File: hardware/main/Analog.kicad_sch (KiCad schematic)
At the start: 51 parts, among them J302 Overvoltage_protection, J303 Rad_sensor, J304 Mos_temp, J305 Mos_temp, U301 INA823DT, U302 INA823DT, U303 INA293A4, U304 INA293A4, U305 TL7726IDR_1

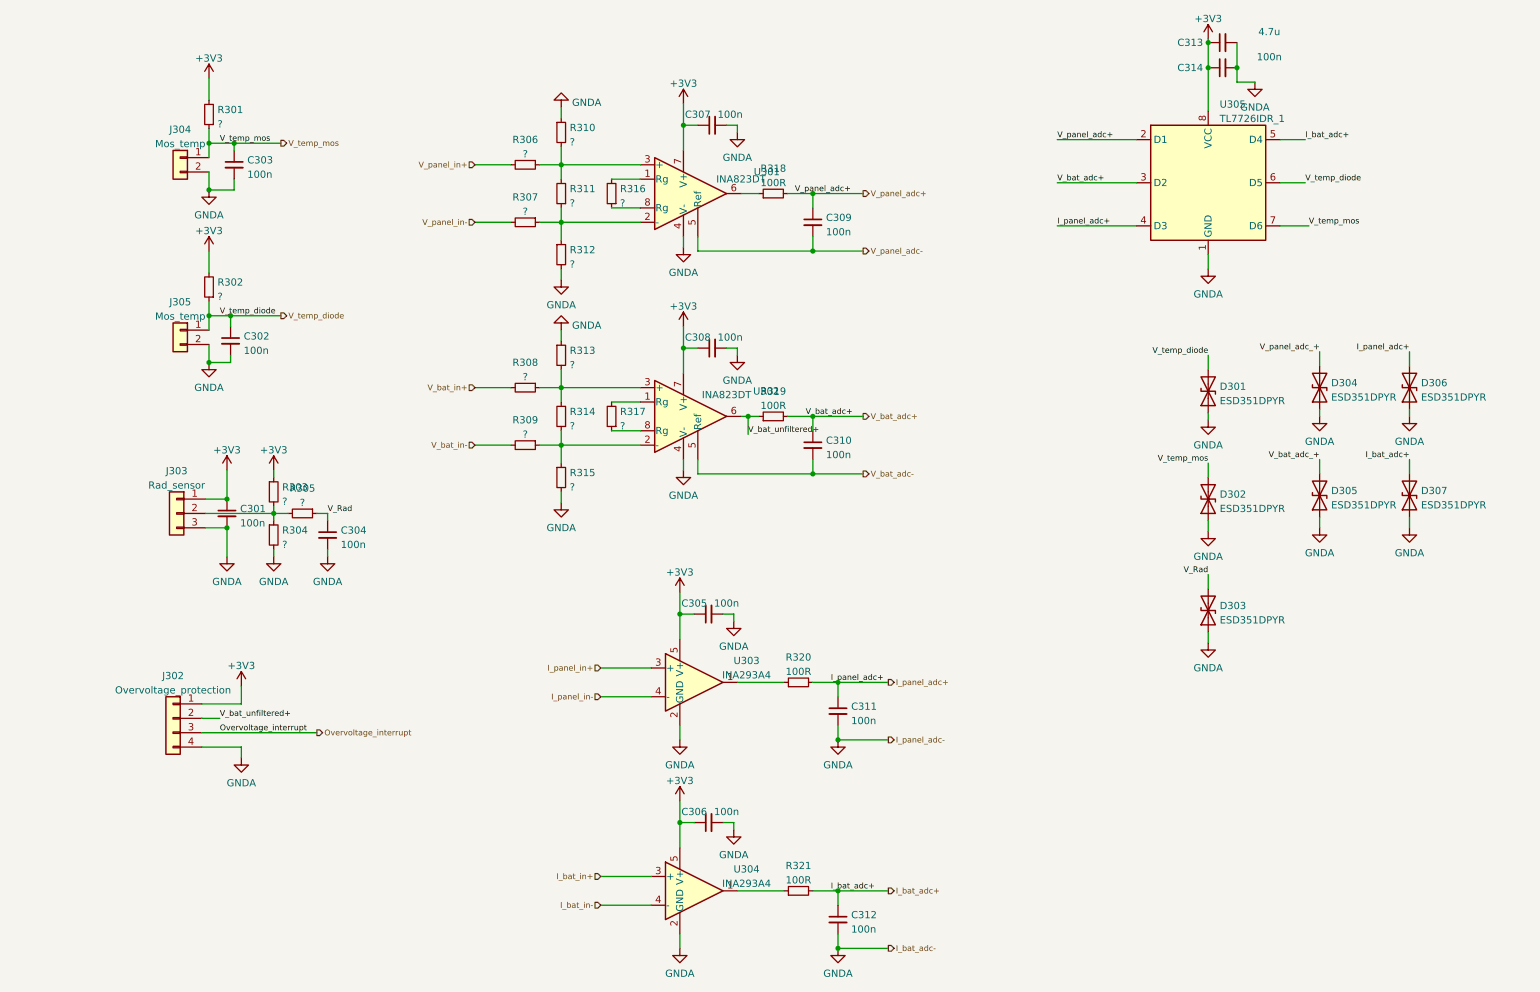
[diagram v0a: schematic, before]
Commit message: Schematics: finalize Analog Snubber and Supplies
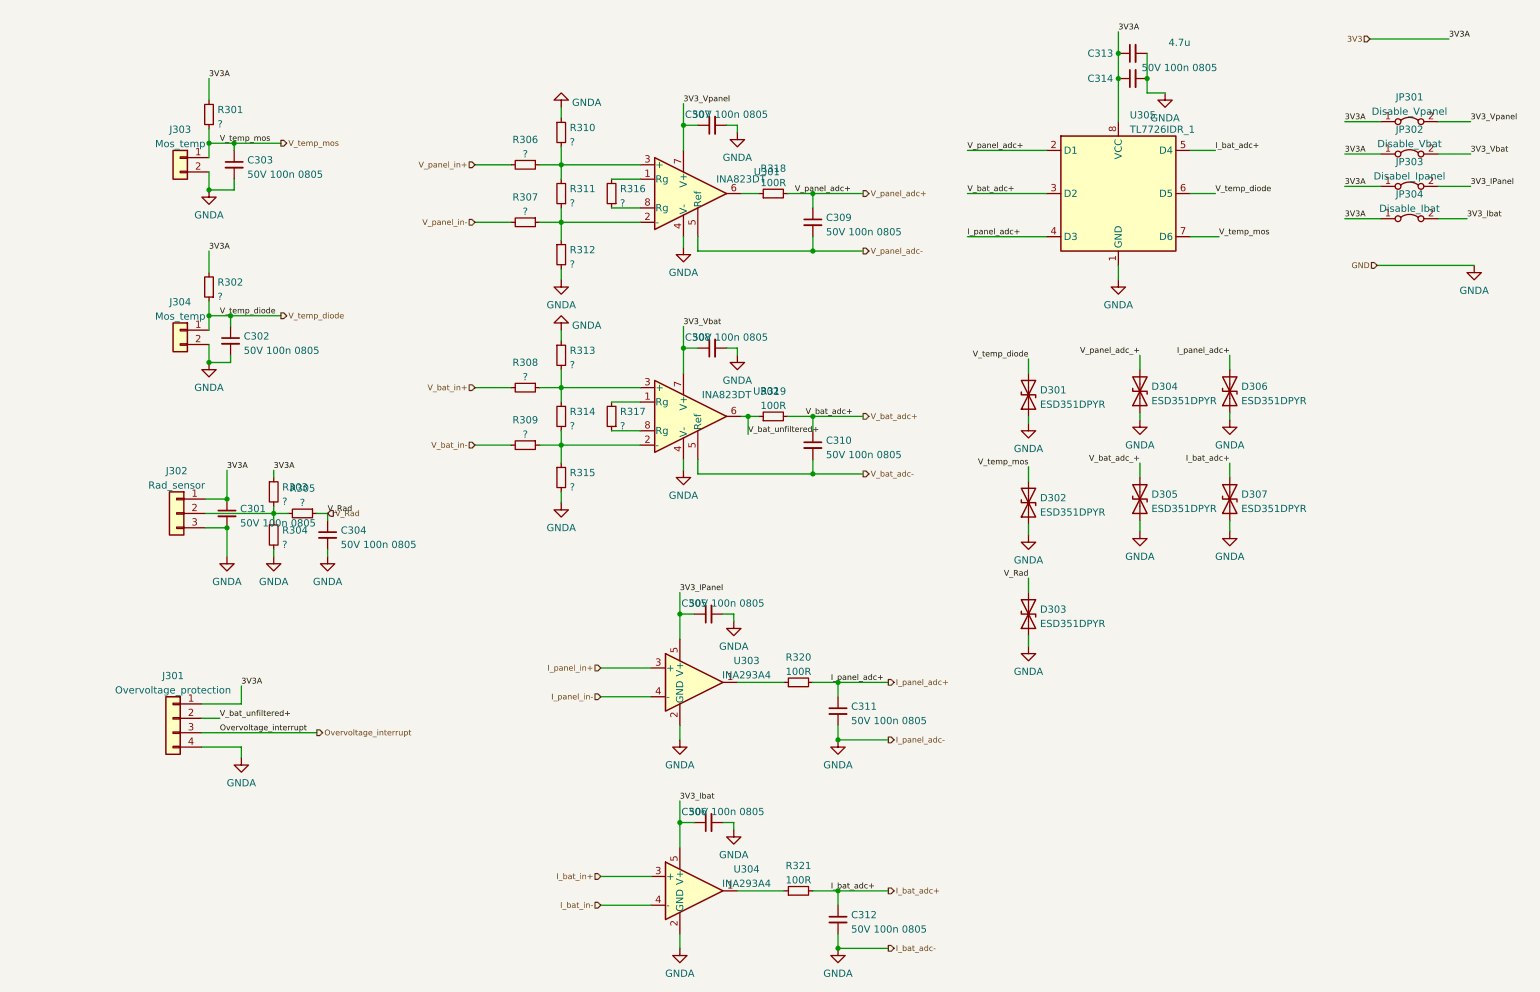
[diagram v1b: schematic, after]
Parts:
- added JP301: Disable_Vpanel, symbol Jumper:Jumper_2_Bridged
- added JP302: Disable_Vbat, symbol Jumper:Jumper_2_Bridged
- added JP303: Disabel_Ipanel, symbol Jumper:Jumper_2_Bridged
- added JP304: Disable_Ibat, symbol Jumper:Jumper_2_Bridged
- C301, C302, C303, C304, C305, C306, C307, C308, C309, C310, C311, C312, C314: value 100n -> 50V 100n 0805
- renumbered J302 to J301, J303 to J302, J304 to J303, J305 to J304
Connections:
- net +3V3 renamed 3V3
- net 3V3: now also JP301.1 (A), JP302.1 (A), JP303.1 (A), JP304.1 (A); no longer C305.1, C306.1, C307.1, C308.1, U301.7 (V+), U302.7 (V+), U303.5 (V+), U304.5 (V+)
- new net 3V3_IPanel: C305.1, JP303.2 (B), U303.5 (V+)
- new net 3V3_Ibat: C306.1, JP304.2 (B), U304.5 (V+)
- new net 3V3_Vbat: C308.1, JP302.2 (B), U302.7 (V+)
- new net 3V3_Vpanel: C307.1, JP301.2 (B), U301.7 (V+)
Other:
- moved on the sheet: C313, C314, D301, D302, D303, D304, D305, D306, D307, U305

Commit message: Schematics: Modified component values
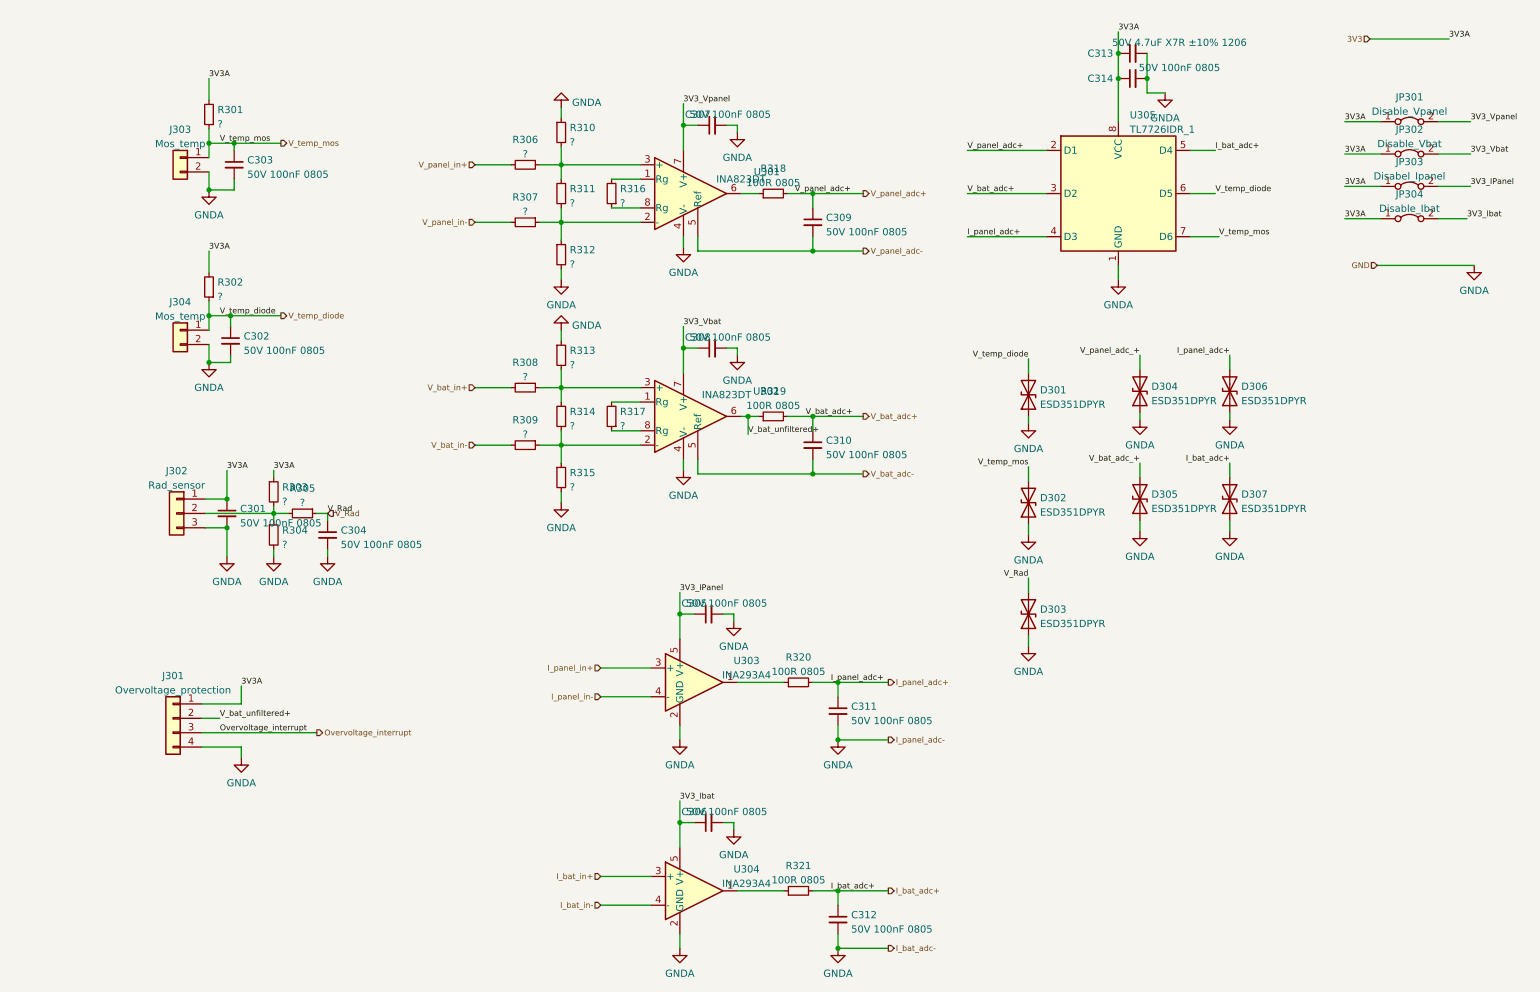
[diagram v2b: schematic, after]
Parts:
- C301, C302, C303, C304, C305, C306, C307, C308, C309, C310, C311, C312, C314: value 50V 100n 0805 -> 50V 100nF 0805
- C313: value 4.7u -> 50V 4.7uF X7R ±10% 1206
- R318, R319, R320, R321: value 100R -> 100R 0805
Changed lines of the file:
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@@
       (effects (font (size 1.27 1.27)) (justify left))
     )
-    (property "Value" "50V 100n 0805" (id 1) (at 68.3641 115.3735 0)
+    (property "Value" "50V 100nF 0805" (id 1) (at 68.3641 115.3735 0)
       (effects (font (size 1.27 1.27)) (justify left))
     )
@@
       (effects (font (size 1.27 1.27)) (justify left))
     )
-    (property "Value" "50V 100n 0805" (id 1) (at 154.0891 60.1285 0)
+    (property "Value" "50V 100nF 0805" (id 1) (at 154.0891 60.1285 0)
       (effects (font (size 1.27 1.27)) (justify left))
     )
@@
       (effects (font (size 1.27 1.27)) (justify left))
     )
-    (property "Value" "50V 100n 0805" (id 1) (at 51.2191 81.0835 0)
+    (property "Value" "50V 100nF 0805" (id 1) (at 51.2191 81.0835 0)
       (effects (font (size 1.27 1.27)) (justify left))
     )
@@
       (effects (font (size 1.27 1.27)) (justify left))
     )
-    (property "Value" "50V 100n 0805" (id 1) (at 50.5841 111.5635 0)
+    (property "Value" "50V 100nF 0805" (id 1) (at 50.5841 111.5635 0)
       (effects (font (size 1.27 1.27)) (justify left))
     )
@@
       (effects (font (size 1.27 1.27)) (justify left))
     )
-    (property "Value" "50V 100n 0805" (id 1) (at 158.5341 183.3185 0)
+    (property "Value" "50V 100nF 0805" (id 1) (at 158.5341 183.3185 0)
       (effects (font (size 1.27 1.27)) (justify left))
     )
@@
       (effects (font (size 1.27 1.27)) (justify left))
     )
-    (property "Value" "50V 100n 0805" (id 1) (at 51.8541 49.9685 0)
+    (property "Value" "50V 100nF 0805" (id 1) (at 51.8541 49.9685 0)
       (effects (font (size 1.27 1.27)) (justify left))
     )
@@
       (effects (font (size 1.27 1.27)) (justify left))
     )
-    (property "Value" "50V 100n 0805" (id 1) (at 154.0891 99.4985 0)
+    (property "Value" "50V 100nF 0805" (id 1) (at 154.0891 99.4985 0)
       (effects (font (size 1.27 1.27)) (justify left))
     )
@@
     (in_bom yes) (on_board yes)
     (property "Reference" "C305" (id 0) (at 130.81 125.73 90))
-    (property "Value" "50V 100n 0805" (id 1) (at 136.525 125.73 90))
+    (property "Value" "50V 100nF 0805" (id 1) (at 136.525 125.73 90))
     (property "Footprint" "" (id 2) (at 133.35 127.635 0)
       (effects (font (size 1.27 1.27)) hide)
@@
     (in_bom yes) (on_board yes) (fields_autoplaced)
     (property "Reference" "R320" (id 0) (at 149.225 135.2636 90))
-    (property "Value" "100R" (id 1) (at 149.225 137.8005 90))
+    (property "Value" "100R 0805" (id 1) (at 149.225 137.8005 90))
     (property "Footprint" "" (id 2) (at 149.225 139.7 0)
       (effects (font (size 1.27 1.27)) hide)
@@
     (in_bom yes) (on_board yes)
     (property "Reference" "C314" (id 0) (at 202.565 33.02 90))
-    (property "Value" "50V 100n 0805" (id 1) (at 216.535 31.115 90))
+    (property "Value" "50V 100nF 0805" (id 1) (at 216.535 31.115 90))
     (property "Footprint" "" (id 2) (at 208.28 33.02 0)
       (effects (font (size 1.27 1.27)) hide)
@@
     (in_bom yes) (on_board yes)
     (property "Reference" "C308" (id 0) (at 131.445 78.74 90))
-    (property "Value" "50V 100n 0805" (id 1) (at 137.16 78.74 90))
+    (property "Value" "50V 100nF 0805" (id 1) (at 137.16 78.74 90))
     (property "Footprint" "" (id 2) (at 133.985 80.645 0)
       (effects (font (size 1.27 1.27)) hide)
@@
     (in_bom yes) (on_board yes)
     (property "Reference" "C307" (id 0) (at 131.445 39.37 90))
-    (property "Value" "50V 100n 0805" (id 1) (at 137.16 39.37 90))
+    (property "Value" "50V 100nF 0805" (id 1) (at 137.16 39.37 90))
     (property "Footprint" "" (id 2) (at 133.985 41.275 0)
       (effects (font (size 1.27 1.27)) hide)
@@
     (in_bom yes) (on_board yes) (fields_autoplaced)
     (property "Reference" "R318" (id 0) (at 144.78 48.9036 90))
-    (property "Value" "100R" (id 1) (at 144.78 51.4405 90))
+    (property "Value" "100R 0805" (id 1) (at 144.78 51.4405 90))
     (property "Footprint" "" (id 2) (at 144.78 53.34 0)
       (effects (font (size 1.27 1.27)) hide)
@@
     (in_bom yes) (on_board yes) (fields_autoplaced)
     (property "Reference" "R321" (id 0) (at 149.225 172.0936 90))
-    (property "Value" "100R" (id 1) (at 149.225 174.6305 90))
+    (property "Value" "100R 0805" (id 1) (at 149.225 174.6305 90))
     (property "Footprint" "" (id 2) (at 149.225 176.53 0)
       (effects (font (size 1.27 1.27)) hide)
@@
       (effects (font (size 1.27 1.27)) (justify left))
     )
-    (property "Value" "50V 100n 0805" (id 1) (at 158.5341 146.4885 0)
+    (property "Value" "50V 100nF 0805" (id 1) (at 158.5341 146.4885 0)
       (effects (font (size 1.27 1.27)) (justify left))
     )
@@
     (in_bom yes) (on_board yes) (fields_autoplaced)
     (property "Reference" "R319" (id 0) (at 144.78 88.2736 90))
-    (property "Value" "100R" (id 1) (at 144.78 90.8105 90))
+    (property "Value" "100R 0805" (id 1) (at 144.78 90.8105 90))
     (property "Footprint" "" (id 2) (at 144.78 92.71 0)
       (effects (font (size 1.27 1.27)) hide)
@@
     (in_bom yes) (on_board yes)
     (property "Reference" "C313" (id 0) (at 202.565 28.575 90))
-    (property "Value" "4.7u" (id 1) (at 216.535 26.67 90))
+    (property "Value" "50V 4.7uF X7R ±10% 1206" (id 1) (at 216.535 26.67 90))
     (property "Footprint" "" (id 2) (at 208.28 28.575 0)
       (effects (font (size 1.27 1.27)) hide)
@@
     (in_bom yes) (on_board yes)
     (property "Reference" "C306" (id 0) (at 130.81 162.56 90))
-    (property "Value" "50V 100n 0805" (id 1) (at 136.525 162.56 90))
+    (property "Value" "50V 100nF 0805" (id 1) (at 136.525 162.56 90))
     (property "Footprint" "" (id 2) (at 133.35 164.465 0)
       (effects (font (size 1.27 1.27)) hide)
